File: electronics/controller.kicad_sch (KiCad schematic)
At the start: 26 parts, among them J1 Conn_01x02, J2 X_Axis_Endstop_Connector, J3 Y_Axis_Endstop_Connector, SW1 EN_Button, SW2 Boot_Button, SW3 Pause/Resume_Button, U1 K7803JT-500R3-LB, U2 LMTOE78_05-0.5, U3 ESP32-S3-WROOM-1

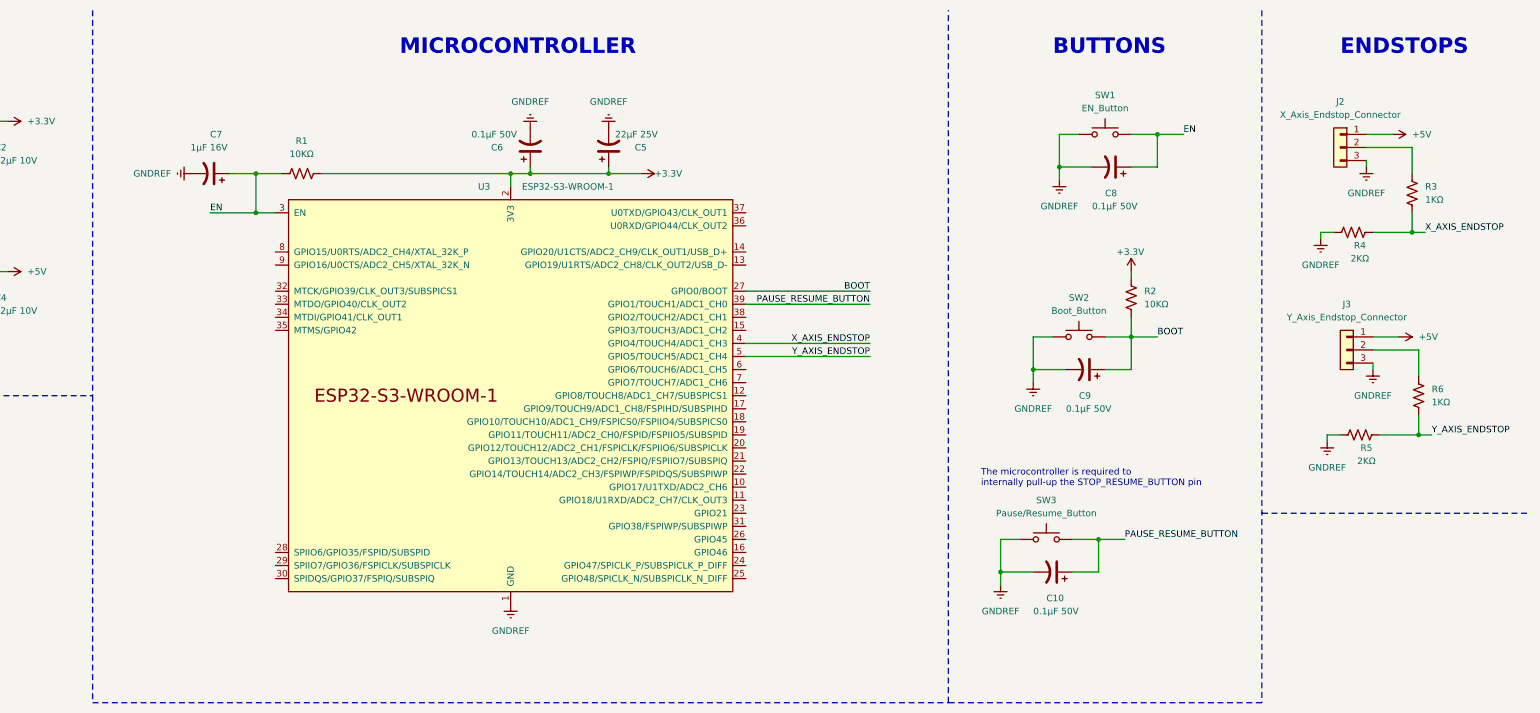
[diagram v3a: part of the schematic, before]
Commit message: ✨ Add MT29F2G01ABAGDWB-IT on KiCad schematic
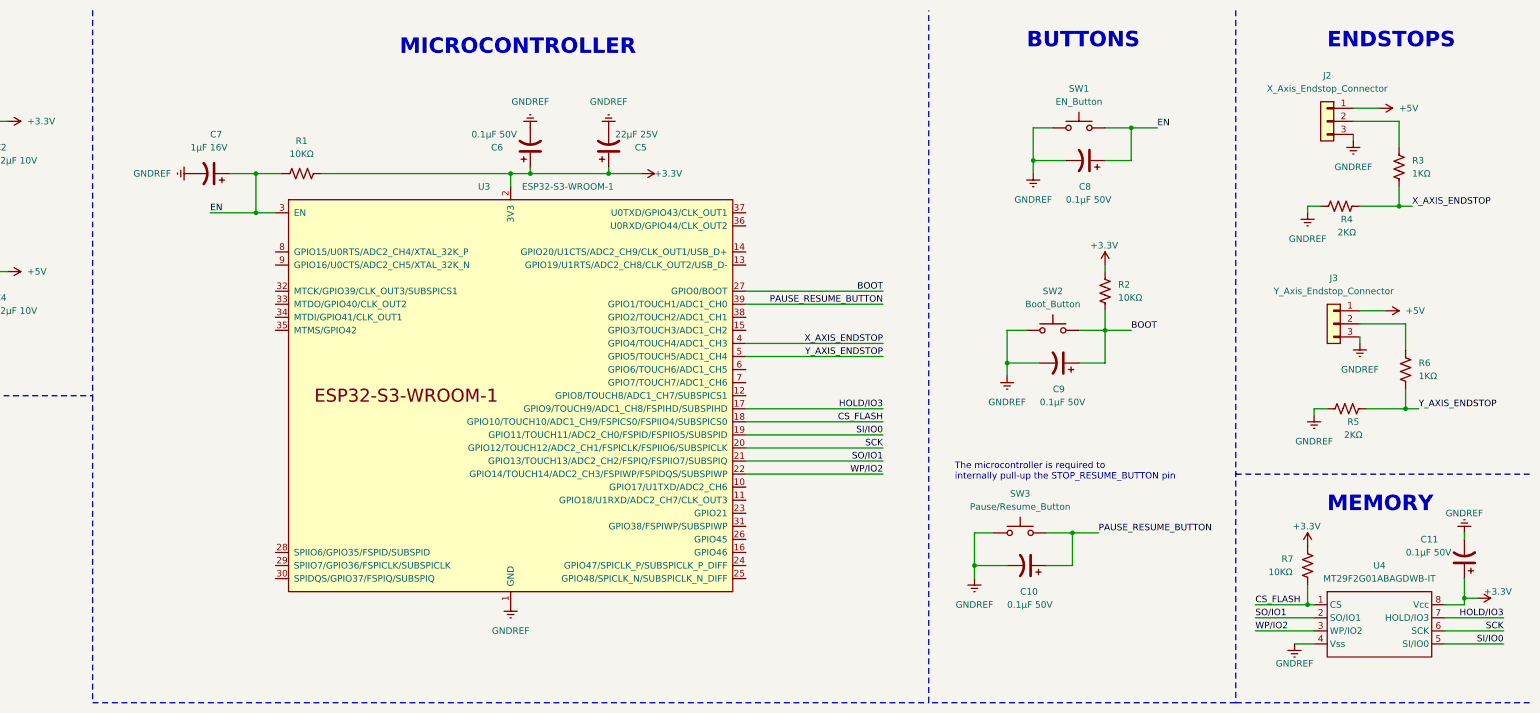
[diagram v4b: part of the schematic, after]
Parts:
- added C11: 0.1µF 50V, symbol Project:C_Polarized_US
- added R7: 10KΩ, symbol Project:R_US
- added U4: MT29F2G01ABAGDWB-IT, symbol Project:MT29F2G01ABAGDWB-IT
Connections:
- net +3.3V: now also C11.1, R7.2, U4.8 (Vcc)
- net GNDREF: now also C11.2, U4.4 (Vss)
- net HOLD/IO3: now reaches U3.17 (GPIO9/TOUCH9/ADC1_CH8/FSPIHD/SUBSPIHD)
- net HOLD/IO3: now also U4.7 (HOLD/IO3)
- net CS_FLASH: now reaches U3.18 (GPIO10/TOUCH10/ADC1_CH9/FSPICS0/FSPIIO4/SUBSPICS0)
- net CS_FLASH: now also R7.1, U4.1 (CS)
- net SI/IO0: now reaches U3.19 (GPIO11/TOUCH11/ADC2_CH0/FSPID/FSPIIO5/SUBSPID)
- net SI/IO0: now also U4.5 (SI/IO0)
- net SCK: now reaches U3.20 (GPIO12/TOUCH12/ADC2_CH1/FSPICLK/FSPIIO6/SUBSPICLK)
- net SCK: now also U4.6 (SCK)
- net SO/IO1: now reaches U3.21 (GPIO13/TOUCH13/ADC2_CH2/FSPIQ/FSPIIO7/SUBSPIQ)
- net SO/IO1: now also U4.2 (SO/IO1)
- net WP/IO2: now reaches U3.22 (GPIO14/TOUCH14/ADC2_CH3/FSPIWP/FSPIDQS/SUBSPIWP)
- net WP/IO2: now also U4.3 (WP/IO2)
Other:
- note added: "MEMORY"
- moved on the sheet: C10, C8, C9, J2, J3, R2, R3, R4, R5, R6, SW1, SW2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

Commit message: ✨ Add USB-C on KiCad schematic
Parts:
- added C12: 0.1µF 10V, symbol Project:C_Polarized_US
- added J4: USB_C_Receptacle_USB2.0, symbol Project:USB_C_Receptacle_USB2.0
- added R10: 2.7KΩ, symbol Project:R_US
- added R11: 4.7KΩ, symbol Project:R_US
- added R8, R9: 5.1KΩ, symbol Project:R_US
- added U5: USBLC6-2SC6, Package_TO_SOT_SMD:SOT-23-6, symbol Project:USBLC6-2SC6
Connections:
- net GNDREF: now also C12.2, J4.A1 (GND), J4.A12 (GND), J4.B1 (GND), J4.B12 (GND), J4.S1 (SHIELD), R11.1, R8.2, R9.2, U5.2 (GND)
- net USB_SENSE: now reaches U3.12 (GPIO8/TOUCH8/ADC1_CH7/SUBSPICS1)
- net USB_SENSE: now also R10.1, R11.2
- net USB_D-: now reaches U3.13 (GPIO19/U1RTS/ADC2_CH8/CLK_OUT2/USB_D-)
- net USB_D-: now also U5.4 (I/O2)
- net USB_D+: now reaches U3.14 (GPIO20/U1CTS/ADC2_CH9/CLK_OUT1/USB_D+)
- net USB_D+: now also U5.6 (I/O1)
- new net: J4.A5 (CC1), R8.1
- new net: J4.A6 (D+), J4.B6 (D+), U5.1 (I/O1)
- new net: J4.A7 (D-), J4.B7 (D-), U5.3 (I/O2)
- new net: J4.B5 (CC2), R9.1
- new net USB_POWER: C12.1, J4.A4 (VBUS), J4.A9 (VBUS), J4.B4 (VBUS), J4.B9 (VBUS), R10.2, U5.5 (VBUS)
- no-connect marks 0 -> 2
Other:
- note added: "USB"
- moved on the sheet: C1, C10, C11, C2, C3, C4, C9, F1, J1, R2, R7, SW2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

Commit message: ✨ Add heaters on KiCad schematic
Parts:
- added J5: Hotend_Connector, symbol Project:Conn_01x02
- added J6: Heated_Bed_Connector, symbol Project:Conn_01x02
- added Q1, Q2: PSMN4R1-30YLC, Package_TO_SOT_SMD:LFPAK56, symbol Project:PSMN4R1-30YLC
- added R12, R15: 10KΩ, symbol Project:R_US
- added R13, R14: 300Ω, symbol Project:R_US
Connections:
- net +24V: now also J5.2 (Pin_2), J6.2 (Pin_2)
- net GNDREF: now also Q1.1 (S), Q1.2 (S), Q1.3 (S), Q2.1 (S), Q2.2 (S), Q2.3 (S), R12.2, R15.2
- net HOTEND_CONTROL: now reaches U3.36 (U0RXD/GPIO44/CLK_OUT2)
- net HOTEND_CONTROL: now also R12.1, R13.1
- net HEATED_BED_CONTROL: now reaches U3.37 (U0TXD/GPIO43/CLK_OUT1)
- net HEATED_BED_CONTROL: now also R14.1, R15.1
- new net: J5.1 (Pin_1), Q1.5 (D)
- new net: Q2.4 (G), R14.2
- new net: J6.1 (Pin_1), Q2.5 (D)
- new net: Q1.4 (G), R13.2
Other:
- note added: "HEATERS"

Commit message: ✨ Add fans on KiCad schematic
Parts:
- added J7: Hotend_Fan_Connector, symbol Project:Conn_01x02
- added J8: Layer_Fan_Connector, symbol Project:Conn_01x02
- added Q3, Q4: PSMN4R1-30YLC, Package_TO_SOT_SMD:LFPAK56, symbol Project:PSMN4R1-30YLC
- added R16, R18: 300Ω, symbol Project:R_US
- added R17, R19: 10KΩ, symbol Project:R_US
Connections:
- net +24V: now also J7.2 (Pin_2), J8.2 (Pin_2)
- net GNDREF: now also Q3.1 (S), Q3.2 (S), Q3.3 (S), Q4.1 (S), Q4.2 (S), Q4.3 (S), R17.2, R19.2
- net HOTEND_FAN_CONTROL: now reaches U3.23 (GPIO21)
- net HOTEND_FAN_CONTROL: now also R16.1, R17.1
- net LAYER_FAN_CONTROL: now reaches U3.25 (GPIO48/SPICLK_N/SUBSPICLK_N_DIFF)
- net LAYER_FAN_CONTROL: now also R18.1, R19.1
- new net: Q4.4 (G), R18.2
- new net: J8.1 (Pin_1), Q4.5 (D)
- new net: J7.1 (Pin_1), Q3.5 (D)
- new net: Q3.4 (G), R16.2
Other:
- note added: "FANS"

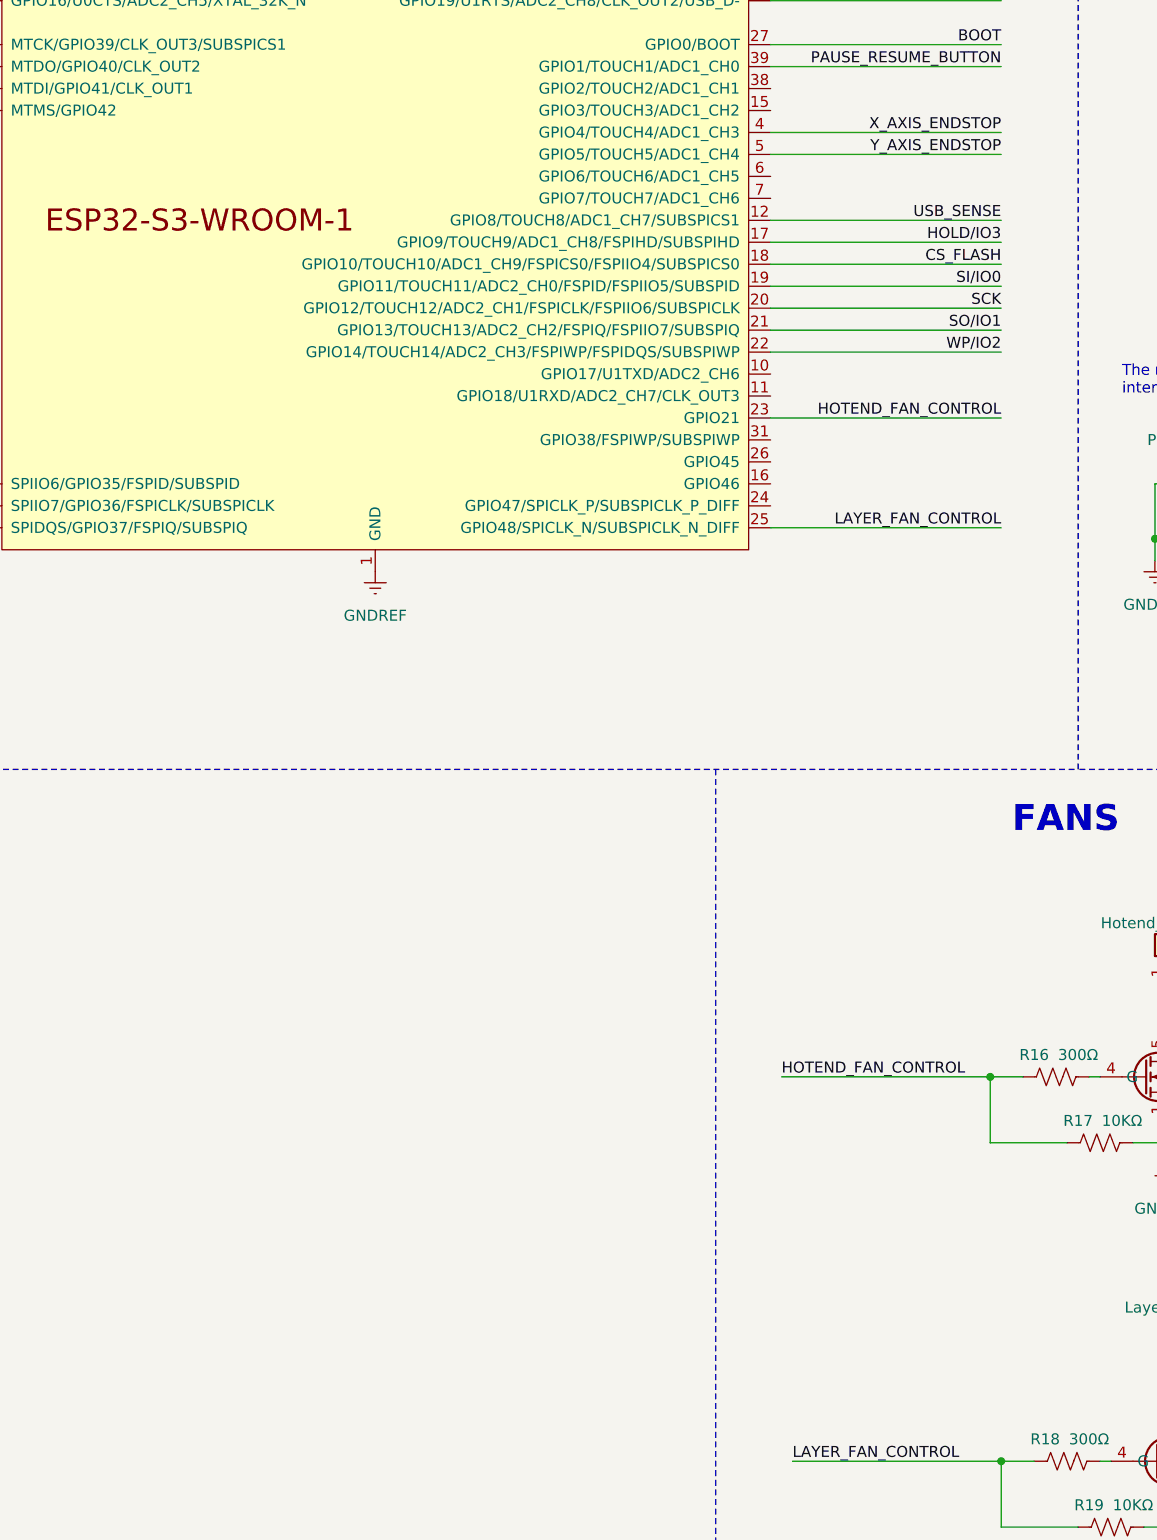
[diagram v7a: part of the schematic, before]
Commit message: ✨ Add thermistors on KiCad schematic
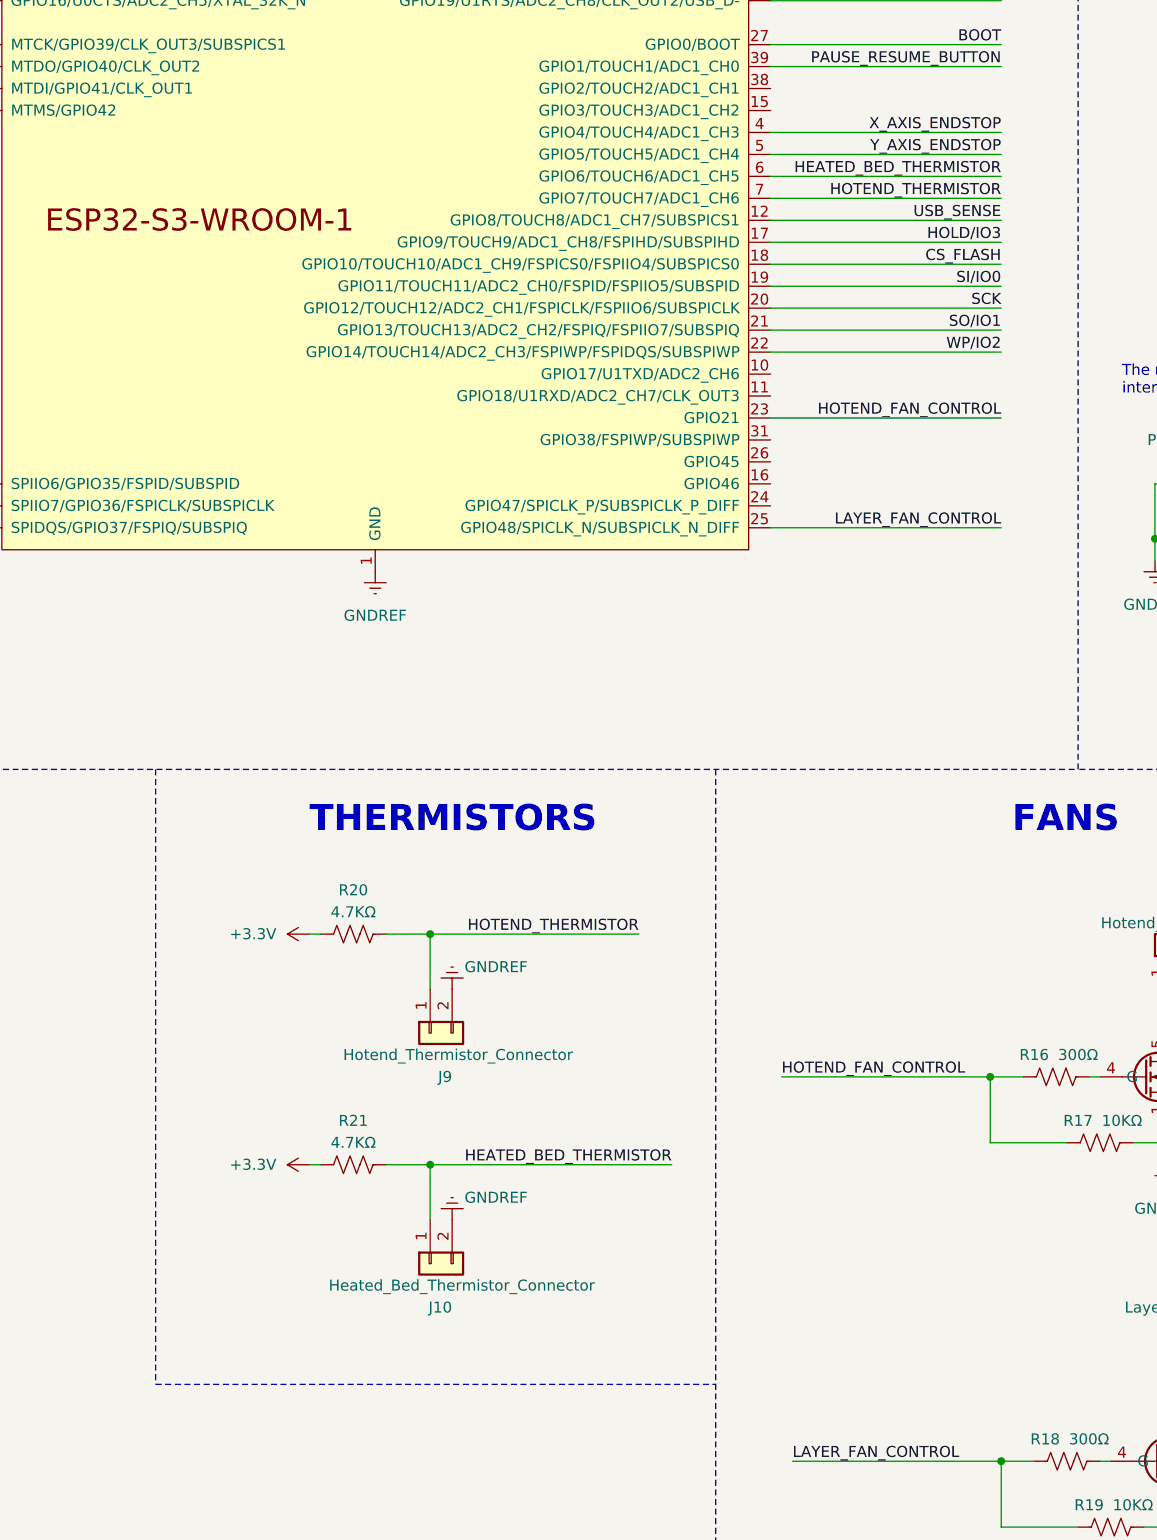
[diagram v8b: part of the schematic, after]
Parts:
- added J10: Heated_Bed_Thermistor_Connector, symbol Project:Conn_01x02
- added J9: Hotend_Thermistor_Connector, symbol Project:Conn_01x02
- added R20, R21: 4.7KΩ, symbol Project:R_US
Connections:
- net +3.3V: now also R20.1, R21.1
- net GNDREF: now also J10.2 (Pin_2), J9.2 (Pin_2)
- net HEATED_BED_THERMISTOR: now reaches U3.6 (GPIO6/TOUCH6/ADC1_CH5)
- net HEATED_BED_THERMISTOR: now also J10.1 (Pin_1), R21.2
- net HOTEND_THERMISTOR: now reaches U3.7 (GPIO7/TOUCH7/ADC1_CH6)
- net HOTEND_THERMISTOR: now also J9.1 (Pin_1), R20.2
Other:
- note added: "THERMISTORS"
